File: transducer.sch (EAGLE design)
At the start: 13 parts

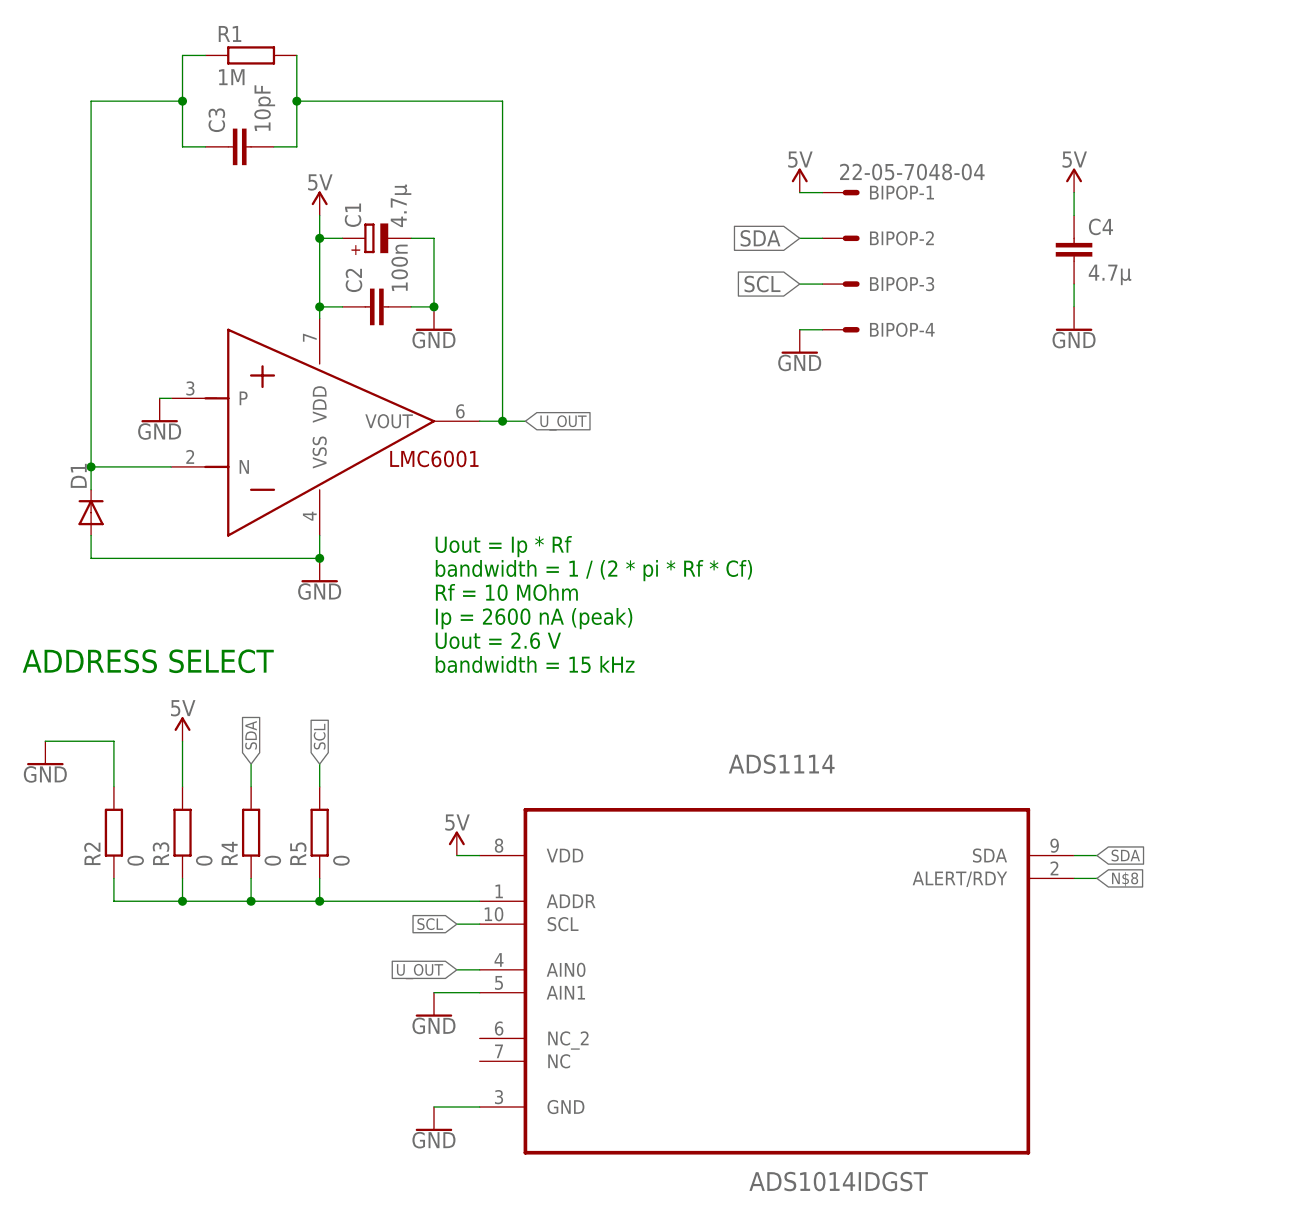
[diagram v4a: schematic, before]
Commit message: SGlux version of transducer, new lib elements, transVIS deleted
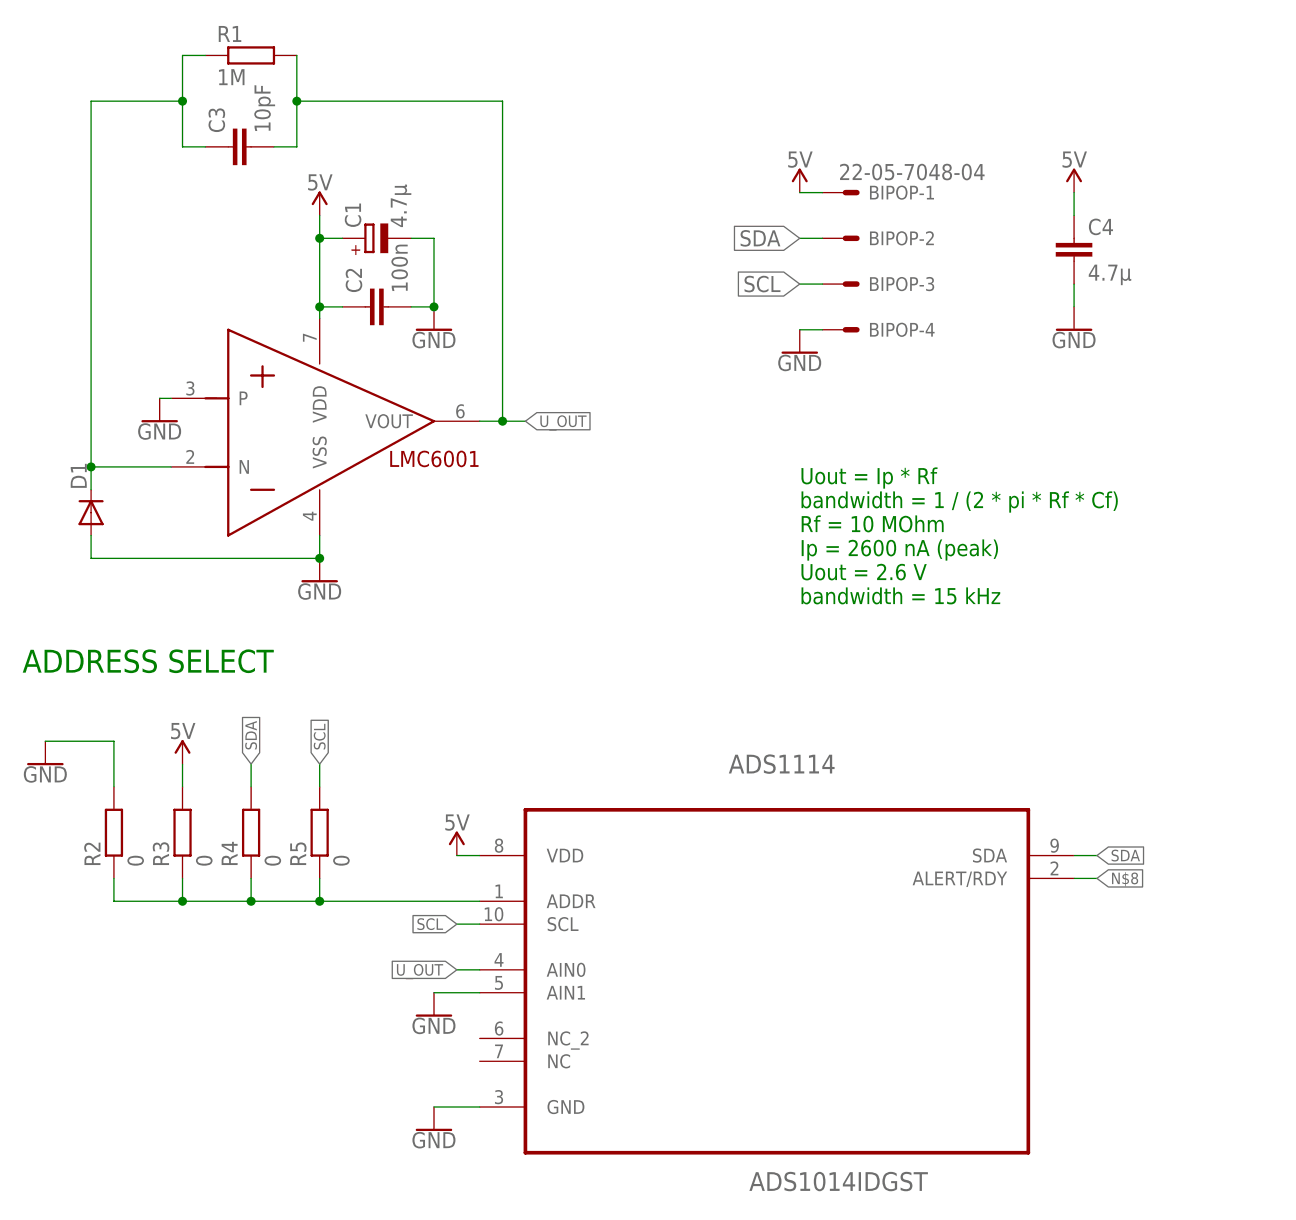
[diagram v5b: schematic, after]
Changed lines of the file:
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@@
 <setting verticaltext="up"/>
 </settings>
-<grid distance="0.1" unitdist="inch" unit="inch" style="lines" multiple="1" display="yes" altdistance="0.01" altunitdist="inch" altunit="inch"/>
+<grid distance="0.1" unitdist="inch" unit="inch" style="lines" multiple="1" display="no" altdistance="0.01" altunitdist="inch" altunit="inch"/>
 <layers>
 <layer number="1" name="Top" color="4" fill="1" visible="no" active="no"/>
@@
 <part name="C3" library="rcl" library_urn="urn:adsk.eagle:library:334" deviceset="C-EU" device="C0603" package3d_urn="urn:adsk.eagle:package:23616/2" value="10pF"/>
 <part name="ADS1114" library="Texas Instruments_By_element14_Batch_1" deviceset="ADS1014IDGST" device=""/>
+<part name="SUPPLY3" library="SparkFun-PowerSymbols" library_urn="urn:adsk.eagle:library:530" deviceset="5V" device=""/>
 <part name="GND4" library="SparkFun-PowerSymbols" library_urn="urn:adsk.eagle:library:530" deviceset="GND" device=""/>
 <part name="GND5" library="SparkFun-PowerSymbols" library_urn="urn:adsk.eagle:library:530" deviceset="GND" device=""/>
+<part name="SUPPLY4" library="SparkFun-PowerSymbols" library_urn="urn:adsk.eagle:library:530" deviceset="5V" device=""/>
 <part name="GND6" library="SparkFun-PowerSymbols" library_urn="urn:adsk.eagle:library:530" deviceset="GND" device=""/>
 <part name="R2" library="rcl" library_urn="urn:adsk.eagle:library:334" deviceset="R-EU_" device="R0805" package3d_urn="urn:adsk.eagle:package:23553/2" value="0"/>
@@
 <part name="GND10" library="SparkFun-PowerSymbols" library_urn="urn:adsk.eagle:library:530" deviceset="GND" device=""/>
 <part name="C4" library="rcl" library_urn="urn:adsk.eagle:library:334" deviceset="C-EU" device="C0805" package3d_urn="urn:adsk.eagle:package:23617/2" value="4.7µ"/>
-<part name="SUPPLY6" library="SparkFun-PowerSymbols" library_urn="urn:adsk.eagle:library:530" deviceset="5V" device=""/>
-<part name="SUPPLY7" library="SparkFun-PowerSymbols" library_urn="urn:adsk.eagle:library:530" deviceset="5V" device=""/>
 </parts>
 <sheets>
 <sheet>
 <plain>
-<text x="68.58" y="22.86" size="1.778" layer="91">Uout = Ip * Rf
+<text x="109.22" y="30.48" size="1.778" layer="91">Uout = Ip * Rf
 bandwidth = 1 / (2 * pi * Rf * Cf)
 Rf = 10 MOhm
@@
 <instance part="C3" gate="G$1" x="45.72" y="81.28" rot="R90"/>
 <instance part="ADS1114" gate="A" x="106.68" y="-7.62"/>
+<instance part="SUPPLY3" gate="G$1" x="71.12" y="2.54"/>
 <instance part="GND4" gate="1" x="68.58" y="-27.94"/>
 <instance part="GND5" gate="1" x="68.58" y="-15.24"/>
+<instance part="SUPPLY4" gate="G$1" x="40.64" y="12.7"/>
 <instance part="GND6" gate="1" x="25.4" y="12.7"/>
 <instance part="R2" gate="G$1" x="33.02" y="5.08" rot="R90"/>
@@
 <instance part="GND10" gate="1" x="139.7" y="60.96"/>
 <instance part="C4" gate="G$1" x="139.7" y="71.12"/>
-<instance part="SUPPLY6" gate="G$1" x="40.64" y="15.24"/>
-<instance part="SUPPLY7" gate="G$1" x="71.12" y="2.54"/>
 </instances>
 <busses>
 </busses>
 <nets>
+<net name="SDA" class="0">
+<segment>
+<pinref part="BIPOP" gate="-2" pin="S"/>
+<wire x1="111.76" y1="71.12" x2="109.22" y2="71.12" width="0.1524" layer="91"/>
+<label x="109.22" y="71.12" size="1.778" layer="95" rot="R180" xref="yes"/>
+</segment>
+<segment>
+<pinref part="ADS1114" gate="A" pin="SDA"/>
+<wire x1="139.7" y1="2.54" x2="142.24" y2="2.54" width="0.1524" layer="91"/>
+<label x="142.24" y="2.54" size="1.27" layer="95" xref="yes"/>
+</segment>
+<segment>
+<wire x1="48.26" y1="12.7" x2="48.26" y2="10.16" width="0.1524" layer="91"/>
+<label x="48.26" y="12.7" size="1.27" layer="95" rot="R90" xref="yes"/>
+<pinref part="R4" gate="G$1" pin="2"/>
+</segment>
+</net>
+<net name="SCL" class="0">
+<segment>
+<pinref part="BIPOP" gate="-3" pin="S"/>
+<wire x1="111.76" y1="66.04" x2="109.22" y2="66.04" width="0.1524" layer="91"/>
+<label x="109.22" y="66.04" size="1.778" layer="95" rot="R180" xref="yes"/>
+</segment>
+<segment>
+<pinref part="ADS1114" gate="A" pin="SCL"/>
+<wire x1="73.66" y1="-5.08" x2="71.12" y2="-5.08" width="0.1524" layer="91"/>
+<label x="71.12" y="-5.08" size="1.27" layer="95" rot="R180" xref="yes"/>
+</segment>
+<segment>
+<wire x1="55.88" y1="12.7" x2="55.88" y2="10.16" width="0.1524" layer="91"/>
+<label x="55.88" y="12.7" size="1.27" layer="95" rot="R90" xref="yes"/>
+<pinref part="R5" gate="G$1" pin="2"/>
+</segment>
+</net>
 <net name="GND" class="0">
 <segment>
@@
 </segment>
 <segment>
+<wire x1="40.64" y1="12.7" x2="40.64" y2="10.16" width="0.1524" layer="91"/>
+<pinref part="SUPPLY4" gate="G$1" pin="5V"/>
+<pinref part="R3" gate="G$1" pin="2"/>
+</segment>
+<segment>
 <pinref part="SUPPLY1" gate="G$1" pin="5V"/>
 <pinref part="LMC6001" gate="G$1" pin="VDD"/>
@@
 </segment>
 <segment>
-<pinref part="R3" gate="G$1" pin="2"/>
-<wire x1="40.64" y1="15.24" x2="40.64" y2="10.16" width="0.1524" layer="91"/>
-<pinref part="SUPPLY6" gate="G$1" pin="5V"/>
-</segment>
-<segment>
 <pinref part="ADS1114" gate="A" pin="VDD"/>
 <wire x1="73.66" y1="2.54" x2="71.12" y2="2.54" width="0.1524" layer="91"/>
-<pinref part="SUPPLY7" gate="G$1" pin="5V"/>
-</segment>
-</net>
-<net name="SDA" class="0">
-<segment>
-<pinref part="BIPOP" gate="-2" pin="S"/>
-<wire x1="111.76" y1="71.12" x2="109.22" y2="71.12" width="0.1524" layer="91"/>
-<label x="109.22" y="71.12" size="1.778" layer="95" rot="R180" xref="yes"/>
-</segment>
-<segment>
-<wire x1="48.26" y1="12.7" x2="48.26" y2="10.16" width="0.1524" layer="91"/>
-<label x="48.26" y="12.7" size="1.27" layer="95" rot="R90" xref="yes"/>
-<pinref part="R4" gate="G$1" pin="2"/>
-</segment>
-<segment>
-<pinref part="ADS1114" gate="A" pin="SDA"/>
-<wire x1="139.7" y1="2.54" x2="142.24" y2="2.54" width="0.1524" layer="91"/>
-<label x="142.24" y="2.54" size="1.27" layer="95" xref="yes"/>
-</segment>
-</net>
-<net name="SCL" class="0">
-<segment>
-<pinref part="BIPOP" gate="-3" pin="S"/>
-<wire x1="111.76" y1="66.04" x2="109.22" y2="66.04" width="0.1524" layer="91"/>
-<label x="109.22" y="66.04" size="1.778" layer="95" rot="R180" xref="yes"/>
-</segment>
-<segment>
-<wire x1="55.88" y1="12.7" x2="55.88" y2="10.16" width="0.1524" layer="91"/>
-<label x="55.88" y="12.7" size="1.27" layer="95" rot="R90" xref="yes"/>
-<pinref part="R5" gate="G$1" pin="2"/>
-</segment>
-<segment>
-<pinref part="ADS1114" gate="A" pin="SCL"/>
-<wire x1="73.66" y1="-5.08" x2="71.12" y2="-5.08" width="0.1524" layer="91"/>
-<label x="71.12" y="-5.08" size="1.27" layer="95" rot="R180" xref="yes"/>
-</segment>
-</net>
+<pinref part="SUPPLY3" gate="G$1" pin="5V"/>
+</segment>
+</net>
